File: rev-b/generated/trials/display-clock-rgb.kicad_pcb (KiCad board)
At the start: 4 copper layers, 136 x 106 mm, 351 parts, among them J1001 LCD RGB / contact fit pending, J1002 CAP TOUCH / contact fit pendi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, J1101 FOOT WIRE: 1SIGNAL 2GND, J1102 FOOT WIRE: 1SIGNAL 2GND, J201 NMJ4HCD2 INPUT, J202 NMJ4HCD2 OUTPUT, J401 PJ-102AH, J501 GOWIN JTAG / target VREF only, J701 UART / POWERED TARGET ONLY, Q401 AO4407A, SW501 RECONFIG / MPN pending, SW701 RESET / SMD button MPN pending, SW702 BOOT / SMD button MPN pending, U101 TPS54302DDCR, U102 TPS54302DDCR, U1101 SN74LVC1G17DCKR, U1102 SN74LVC1G17DCKR, U201 PCM1808PWR, U202 PCM5102APWR, U203 OPA1656IDR, U204 TLV76750DRVR, U205 TLV75533PDBVR, U206 TPS3808G01DBVR, U207 TPS3808G01DBVR, U301 TLV62569DBVR, U302 TPS3897ADRYR, U303 TPS22965DSGR, U501 GW2AR-LV18QN88C8/I7, U502 GD25Q32ESIGR, U503 SN74LVC1G125DCKR, U504 SN74LVC1G17DCKR, U601 TLV62569DBVR, U701 ESP32-P4NRW16X, U702 GD25Q32ESIGR, U801 SN74AXC4T774PWR, U802 TPS3808G01DBVR, U803 SN74LVC1G00DCKR, U901 TPS61169DCKR, U902 SN74LVC1G125DCKR, U903 TLV76701DRVR, U904 TLV76701DRVR, Y501 24.576MHz / 3.3V CMOS XO / MP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, Y701 40MHz / +/-10ppm / MPN and CL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

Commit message: Complete original-pin touch INT source and via-in-pad output trial
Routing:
- net /RGB565 and capacitive touch/TOUCH_INT: track 4.53 -> 63.2 mm, vias 2 -> 4
- net /MCU_TOUCH_INT: track 2.10 -> 24.4 mm, vias 0 -> 6
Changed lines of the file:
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@@
 	)
 	(segment
+		(start 151.75 72)
+		(end 151.75 56.15)
+		(width 0.127)
+		(layer "F.Cu")
+		(net "/RGB565 and capacitive touch/TOUCH_INT")
+	)
+	(segment
 		(start 151.75 55.1)
 		(end 152 54.85)
@@
 	)
 	(segment
+		(start 151.65 72.1)
+		(end 151.75 72)
+		(width 0.127)
+		(layer "F.Cu")
+		(net "/RGB565 and capacitive touch/TOUCH_INT")
+	)
+	(segment
 		(start 152 54.85)
 		(end 152 54.1)
@@
 	)
 	(via
+		(at 118.85 94.3)
+		(size 0.5)
+		(drill 0.3)
+		(layers "F.Cu" "B.Cu")
+		(net "/RGB565 and capacitive touch/TOUCH_INT")
+	)
+	(via
 		(at 152 54.1)
 		(size 0.5)
@@
 		(net "/RGB565 and capacitive touch/TOUCH_INT")
 	)
+	(via
+		(at 151.65 72.1)
+		(size 0.5)
+		(drill 0.3)
+		(layers "F.Cu" "B.Cu")
+		(net "/RGB565 and capacitive touch/TOUCH_INT")
+	)
+	(segment
+		(start 118.9 94.31)
+		(end 118.9 94.3)
+		(width 0.127)
+		(layer "B.Cu")
+		(net "/RGB565 and capacitive touch/TOUCH_INT")
+	)
+	(segment
+		(start 118.9 94.3)
+		(end 118.85 94.3)
+		(width 0.127)
+		(layer "B.Cu")
+		(net "/RGB565 and capacitive touch/TOUCH_INT")
+	)
+	(segment
+		(start 132.65 91.1)
+		(end 151.65 72.1)
+		(width 0.127)
+		(layer "In2.Cu")
+		(net "/RGB565 and capacitive touch/TOUCH_INT")
+	)
+	(segment
+		(start 118.95 94.4)
+		(end 130.35 94.4)
+		(width 0.127)
+		(layer "In2.Cu")
+		(net "/RGB565 and capacitive touch/TOUCH_INT")
+	)
 	(segment
 		(start 152 54.1)
@@
 	)
 	(segment
+		(start 118.85 94.3)
+		(end 118.95 94.4)
+		(width 0.127)
+		(layer "In2.Cu")
+		(net "/RGB565 and capacitive touch/TOUCH_INT")
+	)
+	(segment
+		(start 130.35 94.4)
+		(end 132.65 92.1)
+		(width 0.127)
+		(layer "In2.Cu")
+		(net "/RGB565 and capacitive touch/TOUCH_INT")
+	)
+	(segment
+		(start 132.65 92.1)
+		(end 132.65 91.1)
+		(width 0.127)
+		(layer "In2.Cu")
+		(net "/RGB565 and capacitive touch/TOUCH_INT")
+	)
+	(segment
 		(start 108.1375 86)
 		(end 109 86)
@@
 	)
 	(segment
+		(start 115.15 96.8)
+		(end 115.6 96.35)
+		(width 0.127)
+		(layer "F.Cu")
+		(net "/MCU_TOUCH_INT")
+	)
+	(segment
+		(start 117 87.75)
+		(end 115.7 89.05)
+		(width 0.127)
+		(layer "F.Cu")
+		(net "/MCU_TOUCH_INT")
+	)
+	(segment
+		(start 117 87.575)
+		(end 117 87.75)
+		(width 0.127)
+		(layer "F.Cu")
+		(net "/MCU_TOUCH_INT")
+	)
+	(segment
+		(start 115.7 89.05)
+		(end 114.9 89.05)
+		(width 0.127)
+		(layer "F.Cu")
+		(net "/MCU_TOUCH_INT")
+	)
+	(segment
+		(start 113.6 90)
+		(end 111.35 92.25)
+		(width 0.127)
+		(layer "F.Cu")
+		(net "/MCU_TOUCH_INT")
+	)
+	(segment
 		(start 119.1 87.575)
 		(end 117 87.575)
@@
 		(net "/MCU_TOUCH_INT")
 	)
+	(segment
+		(start 111.45 96.8)
+		(end 115.15 96.8)
+		(width 0.127)
+		(layer "F.Cu")
+		(net "/MCU_TOUCH_INT")
+	)
+	(segment
+		(start 111.35 96.7)
+		(end 111.45 96.8)
+		(width 0.127)
+		(layer "F.Cu")
+		(net "/MCU_TOUCH_INT")
+	)
+	(via
+		(at 114.9 89.05)
+		(size 0.5)
+		(drill 0.3)
+		(layers "F.Cu" "B.Cu")
+		(net "/MCU_TOUCH_INT")
+	)
+	(via
+		(at 115.6 96.35)
+		(size 0.5)
+		(drill 0.3)
+		(layers "F.Cu" "B.Cu")
+		(net "/MCU_TOUCH_INT")
+	)
+	(via
+		(at 111.35 92.25)
+		(size 0.5)
+		(drill 0.3)
+		(layers "F.Cu" "B.Cu")
+		(net "/MCU_TOUCH_INT")
+	)
+	(via
+		(at 118.2 92.75)
+		(size 0.5)
+		(drill 0.3)
+		(layers "F.Cu" "B.Cu")
+		(net "/MCU_TOUCH_INT")
+	)
+	(via
+		(at 113.6 90)
+		(size 0.5)
+		(drill 0.3)
+		(layers "F.Cu" "B.Cu")
+		(net "/MCU_TOUCH_INT")
+	)
+	(via
+		(at 111.35 96.7)
+		(size 0.5)
+		(drill 0.3)
+		(layers "F.Cu" "B.Cu")
+		(net "/MCU_TOUCH_INT")
+	)
+	(segment
+		(start 113.95 90)
+		(end 113.6 90)
+		(width 0.127)
+		(layer "B.Cu")
+		(net "/MCU_TOUCH_INT")
+	)
+	(segment
+		(start 118.35 92.75)
+		(end 118.9 93.3)
+		(width 0.127)
+		(layer "B.Cu")
+		(net "/MCU_TOUCH_INT")
+	)
+	(segment
+		(start 118.9 93.3)
+		(end 118.9 93.29)
+		(width 0.127)
+		(layer "B.Cu")
+		(net "/MCU_TOUCH_INT")
+	)
+	(segment
+		(start 118.2 92.75)
+		(end 118.35 92.75)
+		(width 0.127)
+		(layer "B.Cu")
+		(net "/MCU_TOUCH_INT")
+	)
+	(segment
+		(start 114.9 89.05)
+		(end 113.95 90)
+		(width 0.127)
+		(layer "B.Cu")
+		(net "/MCU_TOUCH_INT")
+	)
+	(segment
+		(start 118.25 92.8)
+		(end 118.2 92.75)
+		(width 0.127)
+		(layer "In2.Cu")
+		(net "/MCU_TOUCH_INT")
+	)
+	(segment
+		(start 111.35 92.25)
+		(end 111.35 96.7)
+		(width 0.127)
+		(layer "In2.Cu")
+		(net "/MCU_TOUCH_INT")
+	)
+	(segment
+		(start 118.25 93.7)
+		(end 118.25 92.8)
+		(width 0.127)
+		(layer "In2.Cu")
+		(net "/MCU_TOUCH_INT")
+	)
+	(segment
+		(start 115.6 96.35)
+		(end 118.25 93.7)
+		(width 0.127)
+		(layer "In2.Cu")
+		(net "/MCU_TOUCH_INT")
+	)

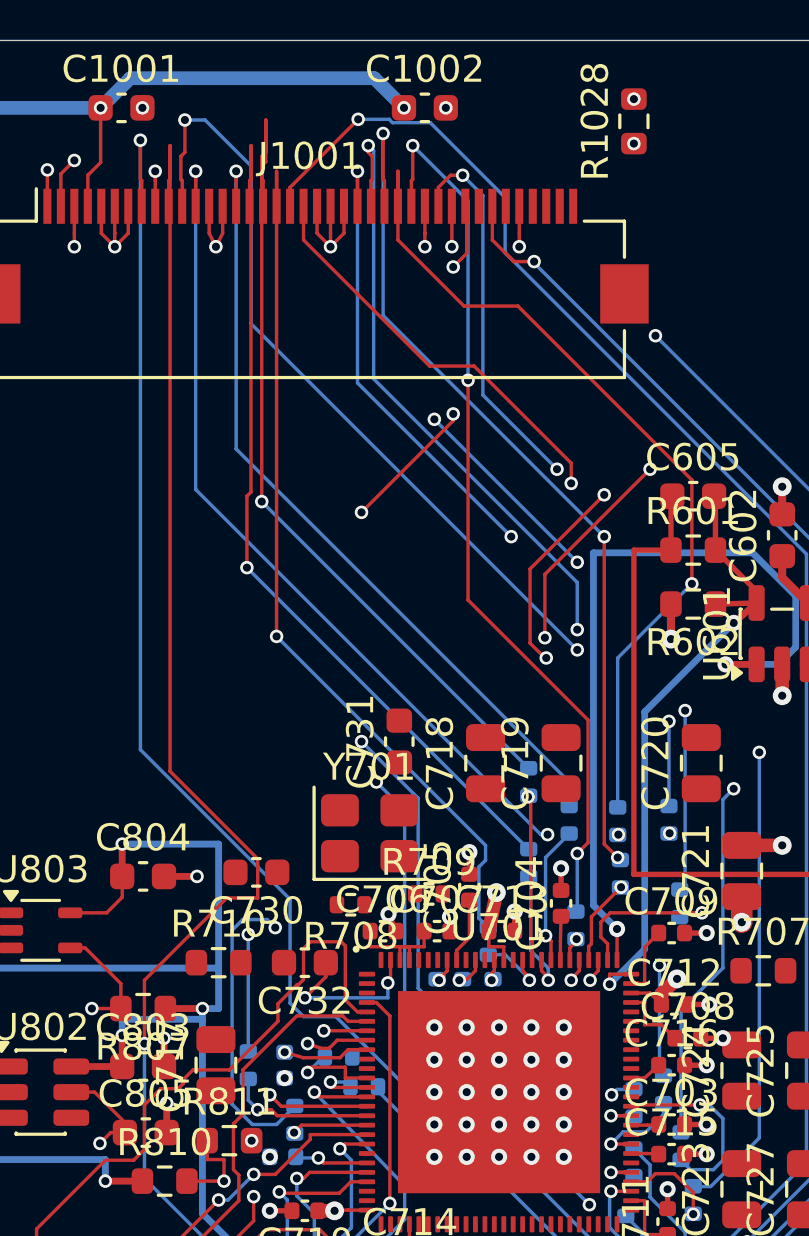
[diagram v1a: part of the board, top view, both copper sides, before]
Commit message: Complete guarded timing and touch fanout with northern VSYNC damping
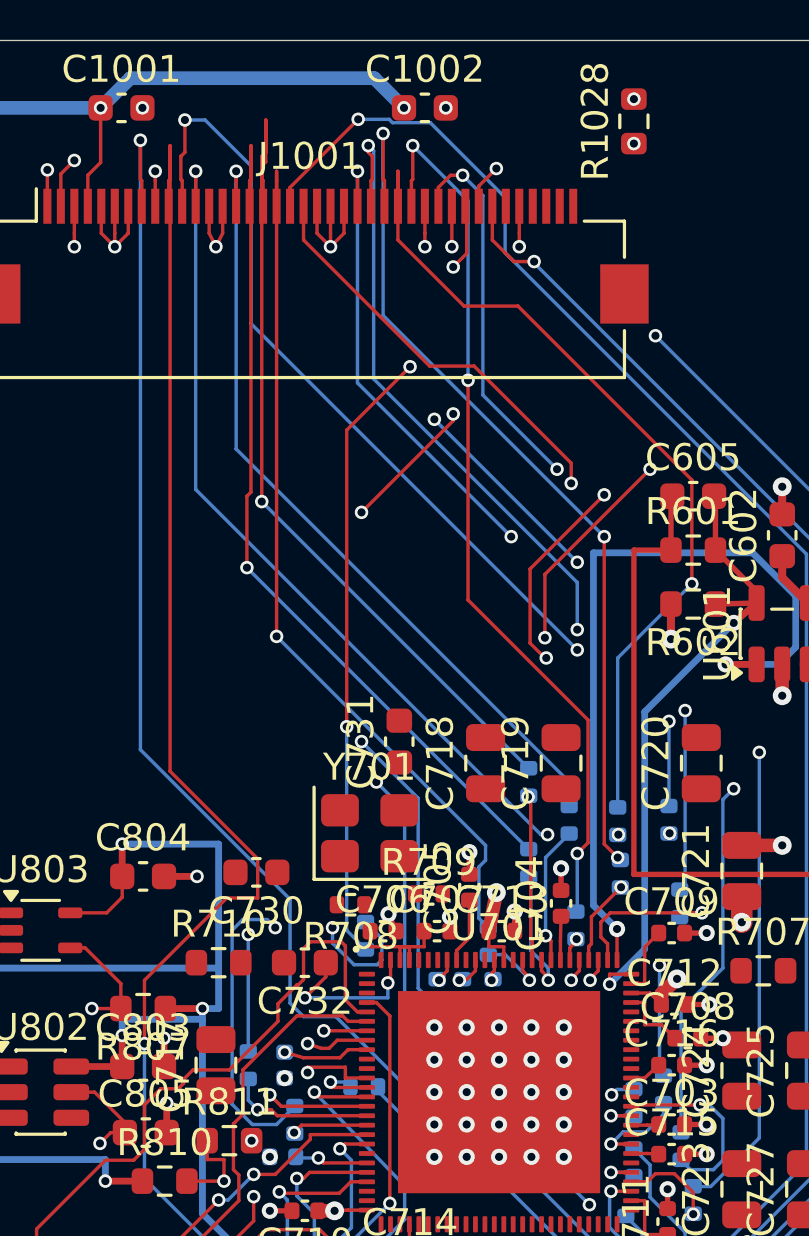
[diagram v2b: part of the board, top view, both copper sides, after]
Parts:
- moved R1019 4.61 mm to (119.0, 80.2), turned to -90 degrees
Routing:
- net /RGB565 and capacitive touch/LCD_VSYNC: track 0.00 -> 33.5 mm, vias 0 -> 3
- net /MCU_LCD_VSYNC: track 3.63 -> 13.2 mm, vias 1 -> 2
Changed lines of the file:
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@@
 	(footprint "KestrelTiming:R_0402_1005Metric_Courtyard0p10"
 		(layer "B.Cu")
-		(at 118.05 84.7)
+		(at 119.05 80.2 -90)
 		(descr "Resistor SMD 0402 (1005 Metric), square (rectangular) end terminal, IPC-7351 nominal, (Body size source: IPC-SM-782 page 72, https://www.pcb-3d.com/wordpress/wp-content/uploads/ipc-sm-782a_amendment_1_and_2.pdf)")
 		(tags "resistor")
 		(property "Reference" "R1019"
-			(at 0 1.17 180)
+			(at 0 1.17 90)
 			(layer "B.SilkS")
 			(effects
@@
 		)
 		(property "Value" "33ohm"
-			(at 0 -1.17 180)
+			(at 0 -1.17 90)
 			(layer "B.Fab")
 			(effects
@@
 		)
 		(property "Datasheet" "https://www.yageogroup.com/component-documentation/download/specsheet/RC0402FR-0733RL"
-			(at 0 0 180)
+			(at 0 0 90)
 			(layer "B.Fab")
 			(hide yes)
@@
 		)
 		(property "Description" ""
-			(at 0 0 180)
+			(at 0 0 90)
 			(layer "B.Fab")
 			(hide yes)
@@
 		)
 		(property "KiLib_Generator" "SMD_2terminal_chip_molded"
-			(at 0 0 180)
+			(at 0 0 90)
 			(layer "B.SilkS")
 			(hide yes)
@@
 		)
 		(property "Manufacturer" "YAGEO"
-			(at 0 0 180)
+			(at 0 0 90)
 			(layer "B.SilkS")
 			(hide yes)
@@
 		)
 		(property "MPN" "RC0402FR-0733RL"
-			(at 0 0 180)
+			(at 0 0 90)
 			(layer "B.SilkS")
 			(hide yes)
@@
 		)
 		(property "LCSC" "C138002"
-			(at 0 0 180)
+			(at 0 0 90)
 			(layer "B.SilkS")
 			(hide yes)
@@
 		)
 		(property "Rating" "33ohm / 1% / 0.063W at 70C / 50V limiting voltage / GPIO source damping starting value"
-			(at 0 0 180)
+			(at 0 0 90)
 			(layer "B.SilkS")
 			(hide yes)
@@
 		)
 		(property "AssemblySide" "B.Cu / source damping passives; assembly qualification pending"
-			(at 0 0 90)
+			(at 0 0 0)
 			(layer "B.SilkS")
 			(hide yes)
@@
 		(duplicate_pad_numbers_are_jumpers no)
 		(fp_line
-			(start -0.153641 -0.38)
-			(end 0.153641 -0.38)
+			(start -0.153641 0.38)
+			(end 0.153641 0.38)
 			(stroke
 				(width 0.12)
@@
 		)
 		(fp_line
-			(start -0.153641 0.38)
-			(end 0.153641 0.38)
+			(start -0.153641 -0.38)
+			(end 0.153641 -0.38)
 			(stroke
 				(width 0.12)
@@
 		)
 		(fp_rect
-			(start -0.88 -0.42)
-			(end 0.88 0.42)
+			(start -0.88 0.42)
+			(end 0.88 -0.42)
 			(stroke
 				(width 0.05)
@@
 		)
 		(fp_text user "${REFERENCE}"
-			(at 0 0 180)
+			(at 0 0 90)
 			(layer "B.Fab")
 			(effects
@@
 		)
 		(pad "1" smd roundrect
-			(at -0.51 0)
+			(at -0.51 0 270)
 			(size 0.54 0.64)
 			(layers "B.Cu" "B.Mask" "B.Paste")
@@
 		)
 		(pad "2" smd roundrect
-			(at 0.51 0)
+			(at 0.51 0 270)
 			(size 0.54 0.64)
 			(layers "B.Cu" "B.Mask" "B.Paste")
@@
 	)
 	(segment
+		(start 118.35 61.45)
+		(end 120.7 59.1)
+		(width 0.127)
+		(layer "F.Cu")
+		(net "/RGB565 and capacitive touch/LCD_VSYNC")
+	)
+	(segment
+		(start 118.35 72.45)
+		(end 118.35 61.45)
+		(width 0.127)
+		(layer "F.Cu")
+		(net "/RGB565 and capacitive touch/LCD_VSYNC")
+	)
+	(segment
+		(start 123.9 51.75)
+		(end 123.25 52.4)
+		(width 0.127)
+		(layer "F.Cu")
+		(net "/RGB565 and capacitive touch/LCD_VSYNC")
+	)
+	(segment
+		(start 123.25 52.4)
+		(end 123.25 53.15)
+		(width 0.127)
+		(layer "F.Cu")
+		(net "/RGB565 and capacitive touch/LCD_VSYNC")
+	)
+	(via
+		(at 118.35 72.45)
+		(size 0.5)
+		(drill 0.3)
+		(layers "F.Cu" "B.Cu")
+		(net "/RGB565 and capacitive touch/LCD_VSYNC")
+	)
+	(via
+		(at 120.7 59.1)
+		(size 0.5)
+		(drill 0.3)
+		(layers "F.Cu" "B.Cu")
+		(net "/RGB565 and capacitive touch/LCD_VSYNC")
+	)
+	(via
+		(at 123.9 51.75)
+		(size 0.5)
+		(drill 0.3)
+		(layers "F.Cu" "B.Cu")
+		(net "/RGB565 and capacitive touch/LCD_VSYNC")
+	)
+	(segment
+		(start 119.05 80.71)
+		(end 119.05 80.7)
+		(width 0.127)
+		(layer "B.Cu")
+		(net "/RGB565 and capacitive touch/LCD_VSYNC")
+	)
+	(segment
+		(start 118.35 80)
+		(end 118.35 72.45)
+		(width 0.127)
+		(layer "B.Cu")
+		(net "/RGB565 and capacitive touch/LCD_VSYNC")
+	)
+	(segment
+		(start 119.05 80.7)
+		(end 118.35 80)
+		(width 0.127)
+		(layer "B.Cu")
+		(net "/RGB565 and capacitive touch/LCD_VSYNC")
+	)
+	(segment
+		(start 120.7 59.1)
+		(end 120.7 54.45)
+		(width 0.127)
+		(layer "In2.Cu")
+		(net "/RGB565 and capacitive touch/LCD_VSYNC")
+	)
+	(segment
+		(start 120.7 54.45)
+		(end 122.6 52.55)
+		(width 0.127)
+		(layer "In2.Cu")
+		(net "/RGB565 and capacitive touch/LCD_VSYNC")
+	)
+	(segment
+		(start 122.6 52.55)
+		(end 123.1 52.55)
+		(width 0.127)
+		(layer "In2.Cu")
+		(net "/RGB565 and capacitive touch/LCD_VSYNC")
+	)
+	(segment
+		(start 123.1 52.55)
+		(end 123.9 51.75)
+		(width 0.127)
+		(layer "In2.Cu")
+		(net "/RGB565 and capacitive touch/LCD_VSYNC")
+	)
+	(segment
 		(start 124.55 55.2)
 		(end 123.75 54.4)
@@
 		(net "/MCU_LCD_VSYNC")
 	)
+	(via
+		(at 117.825 79.9)
+		(size 0.5)
+		(drill 0.3)
+		(layers "F.Cu" "B.Cu")
+		(net "/MCU_LCD_VSYNC")
+	)
 	(segment
-		(start 117.475 84.7)
-		(end 117.49 84.7)
+		(start 119.475 81.275)
+		(end 119.65 81.1)
 		(width 0.127)
 		(layer "B.Cu")
@@
 	)
 	(segment
-		(start 116.9 85.275)
-		(end 117.475 84.7)
+		(start 119.05 79.7)
+		(end 119.05 79.69)
 		(width 0.127)
 		(layer "B.Cu")
 		(net "/MCU_LCD_VSYNC")
 	)
+	(segment
+		(start 119.65 81.1)
+		(end 119.65 80.3)
+		(width 0.127)
+		(layer "B.Cu")
+		(net "/MCU_LCD_VSYNC")
+	)
+	(segment
+		(start 119.65 80.3)
+		(end 119.05 79.7)
+		(width 0.127)
+		(layer "B.Cu")
+		(net "/MCU_LCD_VSYNC")
+	)
+	(segment
+		(start 117.825 80.475)
+		(end 118.625 81.275)
+		(width 0.127)
+		(layer "B.Cu")
+		(net "/MCU_LCD_VSYNC")
+	)
+	(segment
+		(start 118.625 81.275)
+		(end 119.475 81.275)
+		(width 0.127)
+		(layer "B.Cu")
+		(net "/MCU_LCD_VSYNC")
+	)
+	(segment
+		(start 117.825 79.9)
+		(end 117.825 80.475)
+		(width 0.127)
+		(layer "B.Cu")
+		(net "/MCU_LCD_VSYNC")
+	)
+	(segment
+		(start 118.025 84.15)
+		(end 118.025 80.1)
+		(width 0.127)
+		(layer "In2.Cu")
+		(net "/MCU_LCD_VSYNC")
+	)
+	(segment
+		(start 118.025 80.1)
+		(end 117.825 79.9)
+		(width 0.127)
+		(layer "In2.Cu")
+		(net "/MCU_LCD_VSYNC")
+	)
+	(segment
+		(start 116.9 85.275)
+		(end 118.025 84.15)
+		(width 0.127)
+		(layer "In2.Cu")
+		(net "/MCU_LCD_VSYNC")
+	)

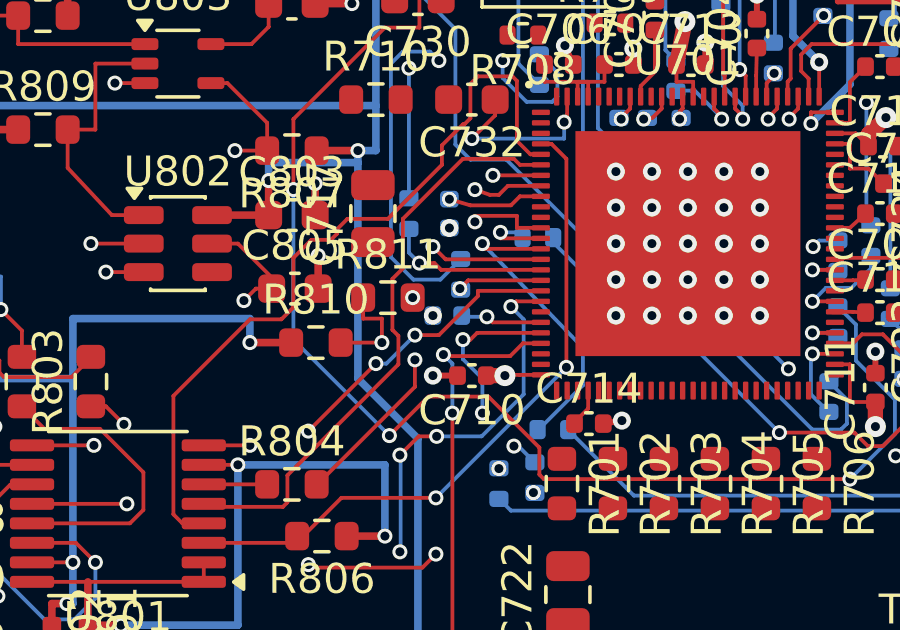
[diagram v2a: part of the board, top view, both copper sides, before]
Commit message: Bring C702 trial bypass allocation within maintained bound
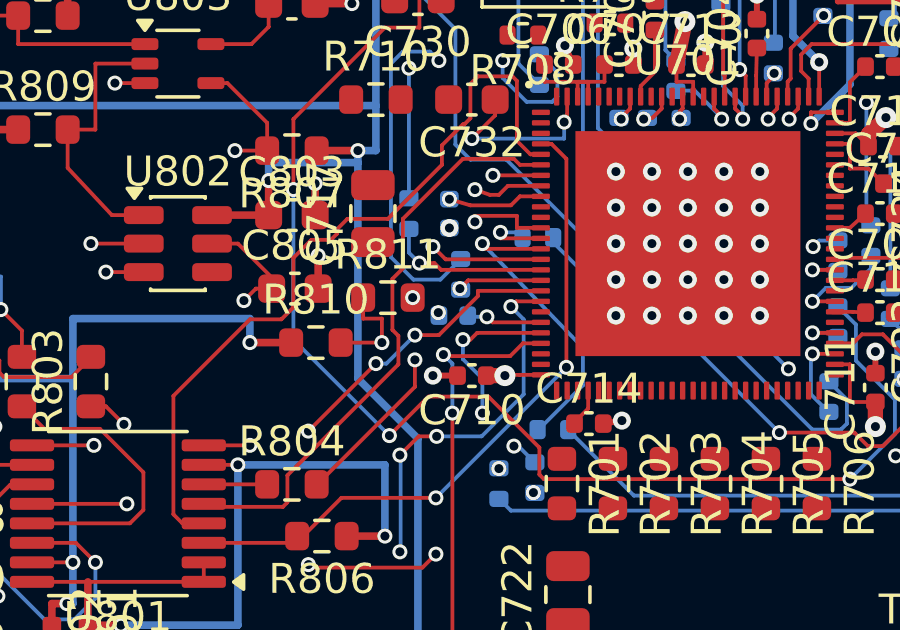
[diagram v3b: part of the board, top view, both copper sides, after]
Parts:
- moved C702 0.20 mm to (116.2, 88.4)
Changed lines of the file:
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@@
 	(footprint "Capacitor_SMD:C_0402_1005Metric"
 		(layer "B.Cu")
-		(at 115.98 88.4 180)
+		(at 116.18 88.4 180)
 		(descr "Capacitor SMD 0402 (1005 Metric), square (rectangular) end terminal, IPC-7351 nominal, (Body size source: IPC-SM-782 page 76, https://www.pcb-3d.com/wordpress/wp-content/uploads/ipc-sm-782a_amendment_1_and_2.pdf)")
 		(tags "capacitor")
@@
 	(segment
 		(start 116.5 88.44)
-		(end 116.46 88.4)
+		(end 116.66 88.4)
 		(width 0.127)
 		(layer "B.Cu")
@@
 	)
 	(via
-		(at 115.5 88.4)
-		(size 0.6)
+		(at 115.68 88.3)
+		(size 0.5)
 		(drill 0.3)
 		(layers "F.Cu" "B.Cu")
